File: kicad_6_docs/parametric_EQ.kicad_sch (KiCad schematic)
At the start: 12 parts

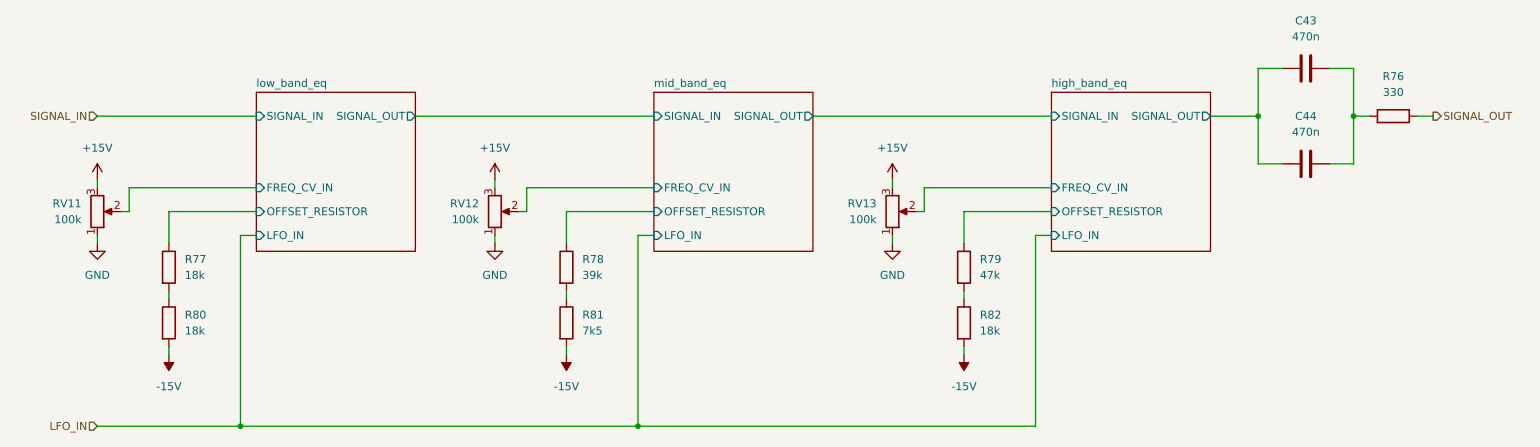
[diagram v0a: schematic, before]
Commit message: Fix power supply errors, tidy up schematic
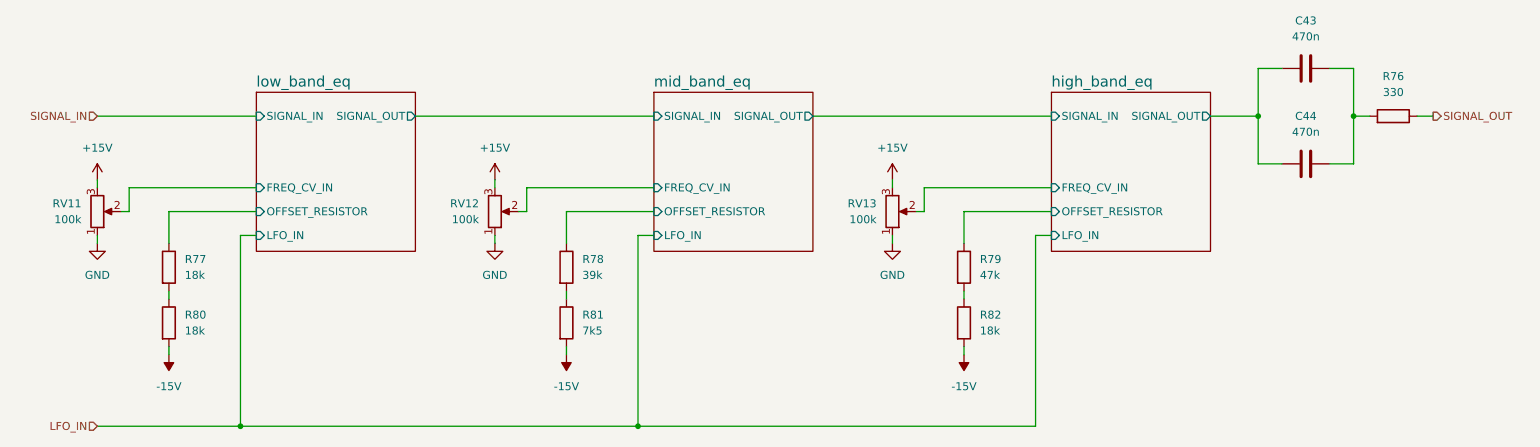
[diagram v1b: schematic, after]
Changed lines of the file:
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@@
   (title_block
     (title "Wiggly EQ")
-    (date "2022-05-29")
+    (date "2022-08-01")
     (rev "0")
     (comment 2 "creativecommons.org/licenses/by/4.0")
@@
     (fill (color 0 0 0 0.0000))
     (property "Sheet name" "low_band_eq" (id 0) (at 74.93 78.0284 0)
-      (effects (font (size 1.27 1.27)) (justify left bottom))
+      (effects (font (size 1.7 1.7)) (justify left bottom))
     )
     (property "Sheet file" "parametric_eq_stage.kicad_sch" (id 1) (at 74.93 104.7246 0)
@@
     (fill (color 0 0 0 0.0000))
     (property "Sheet name" "high_band_eq" (id 0) (at 201.93 78.0284 0)
-      (effects (font (size 1.27 1.27)) (justify left bottom))
+      (effects (font (size 1.7 1.7)) (justify left bottom))
     )
     (property "Sheet file" "parametric_eq_stage.kicad_sch" (id 1) (at 201.93 104.7246 0)
@@
     (fill (color 0 0 0 0.0000))
     (property "Sheet name" "mid_band_eq" (id 0) (at 138.43 78.0284 0)
-      (effects (font (size 1.27 1.27)) (justify left bottom))
+      (effects (font (size 1.7 1.7)) (justify left bottom))
     )
     (property "Sheet file" "parametric_eq_stage.kicad_sch" (id 1) (at 138.43 104.7246 0)
